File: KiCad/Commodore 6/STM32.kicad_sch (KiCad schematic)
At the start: 13 parts, among them J1 472192001, U1 STM32H562RIT6, U2 STM32H7A3RIT6

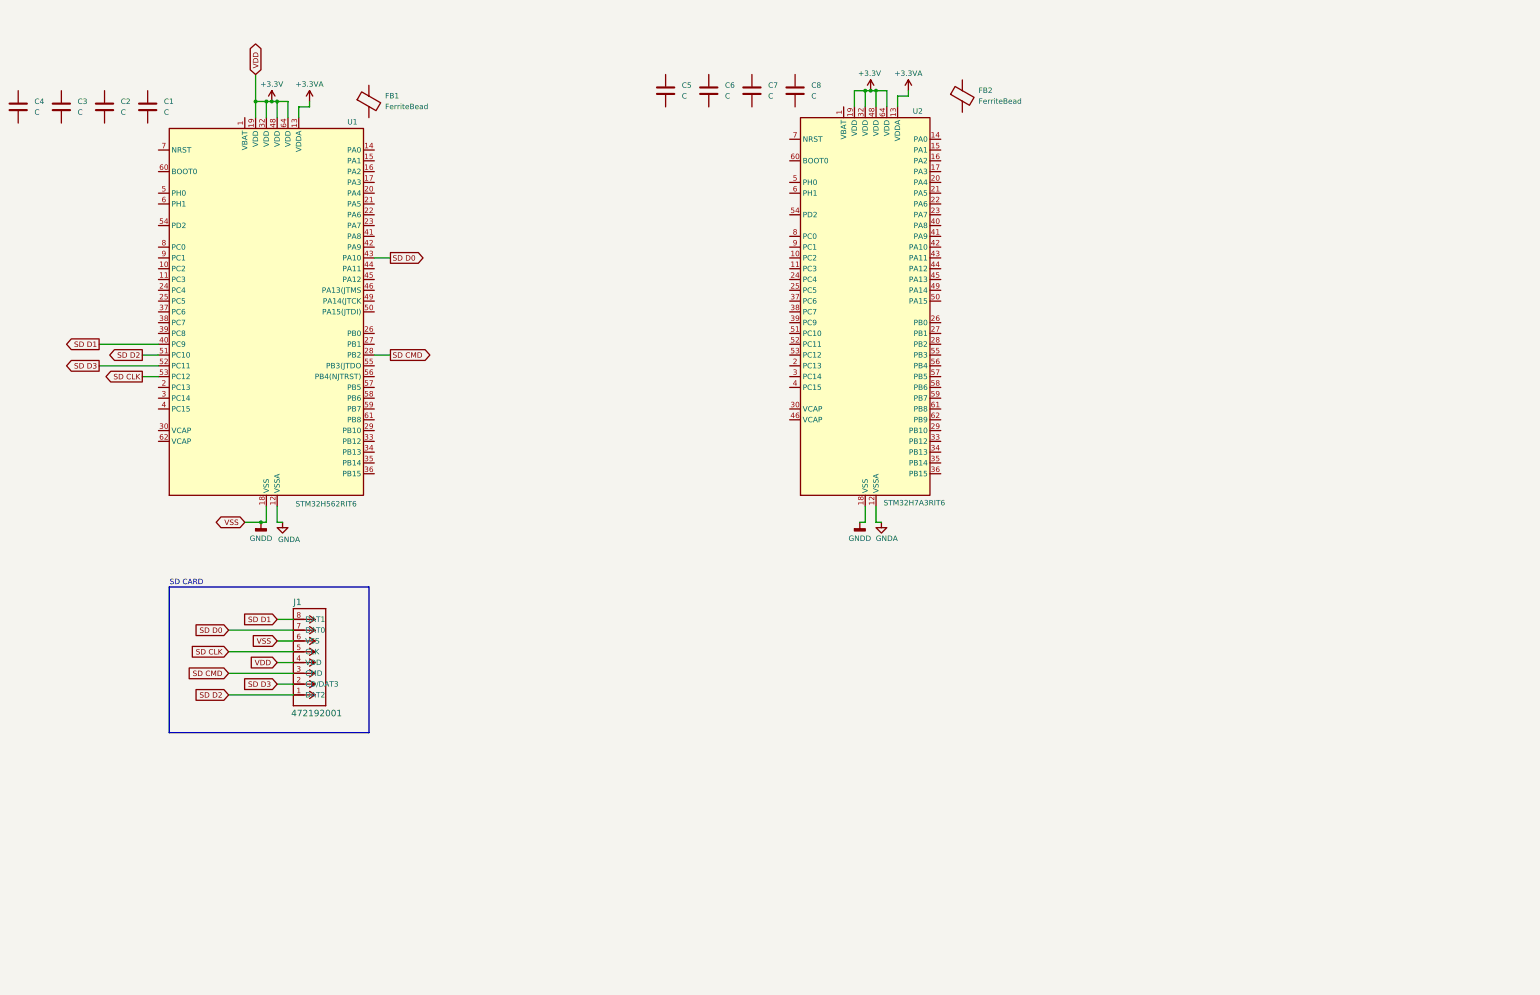
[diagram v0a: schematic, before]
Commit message: Added Ferite Bead
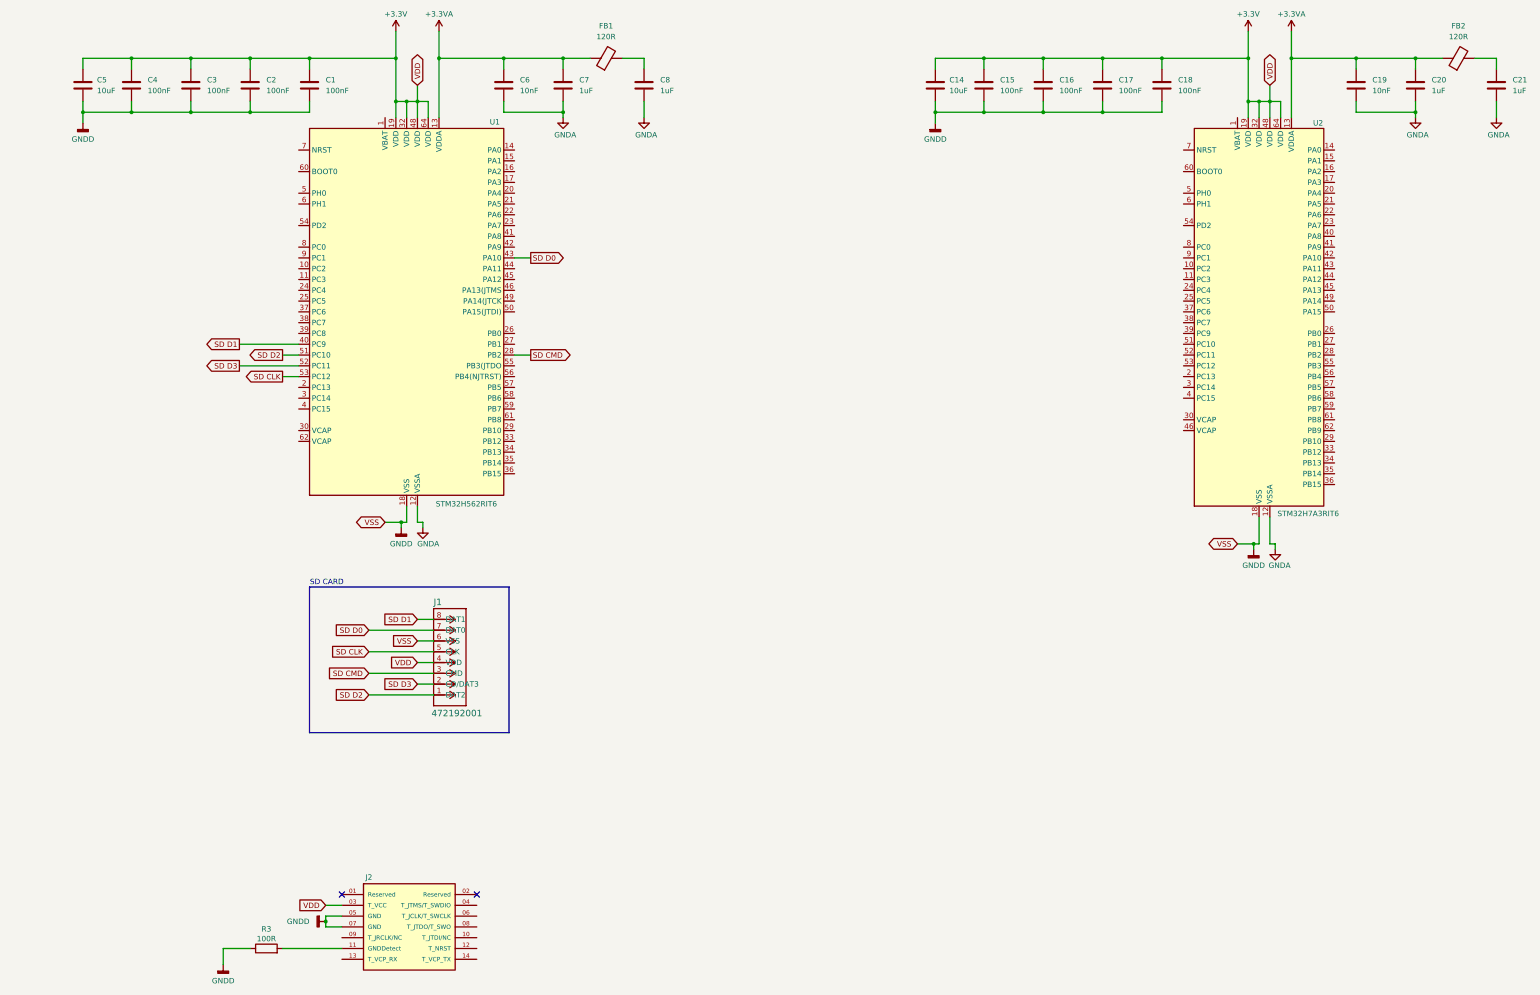
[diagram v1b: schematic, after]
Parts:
- added C14: 10uF, symbol Device:C
- added C15, C16, C17, C18: 100nF, symbol Device:C
- added C19: 10nF, symbol Device:C
- added C20, C21: 1uF, symbol Device:C
- added J2: FTSH-107-01-L-DV-K-A, FTSH-107-01-L-DV-K-A:SAMTEC_FTSH-107-01-L-DV-K-A, symbol FTSH_107_01_L_DV_K_A SWD Connecter:FTSH-107-01-L-DV-K-A
- added R3: 100R, symbol Device:R
- C1, C2, C3, C4: value C -> 100nF
- C5: value C -> 10uF
- C6: value C -> 10nF
- C7, C8: value C -> 1uF
- FB1, FB2: value FerriteBead -> 120R
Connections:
- net +3.3V: now also C1.1, C2.1, C3.1, C4.1, C5.1, C14.1, C15.1, C16.1, C17.1, C18.1, J2.03 (T_VCC)
- net +3.3VA: now also C6.1, C7.1, FB1.1, FB2.1, C19.1, C20.1
- net GNDA: now also C6.2, C7.2, C8.2, C19.2, C20.2, C21.2
- net GNDD: now also C1.2, C2.2, C3.2, C4.2, C5.2, C14.2, C15.2, C16.2, C17.2, C18.2, J2.05 (GND), J2.07 (GND), R3.1
- net at FB2.2: now also C21.1
- net at C8.1: now also FB1.2
- new net: J2.11 (GNDDetect), R3.2
- no-connect marks 0 -> 2
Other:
- moved on the sheet: C1, C2, C3, C4, C5, FB1, J1, U1, U2
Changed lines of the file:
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@@
 	(generator "eeschema")
 	(generator_version "9.0")
-	(paper "A3")
+	(paper "A2")

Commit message: I'm Tired
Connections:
- net T_SWDIO: now reaches U1.46 (PA13(JTMS)
- net T_SWDIO: now also J2.04 (T_JTMS/T_SWDIO)
- net T_SWCLK: now reaches U1.49 (PA14(JTCK)
- net T_SWCLK: now also J2.06 (T_JCLK/T_SWCLK)
- net T_JTDI: now reaches U1.50 (PA15(JTDI))
- net T_JTDI: now also J2.10 (T_JTDI/NC)
- net T_SWO: now reaches U1.55 (PB3(JTDO)
- net T_SWO: now also J2.08 (T_JTDO/T_SWO)
- net T_NRST: now reaches U1.7 (NRST)
- net T_NRST: now also J2.12 (T_NRST)
- net T_VCP_RX: now reaches J2.13 (T_VCP_RX)
- net T_VCP_TX: now reaches J2.14 (T_VCP_TX)
- no-connect marks 2 -> 3
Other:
- moved on the sheet: R3

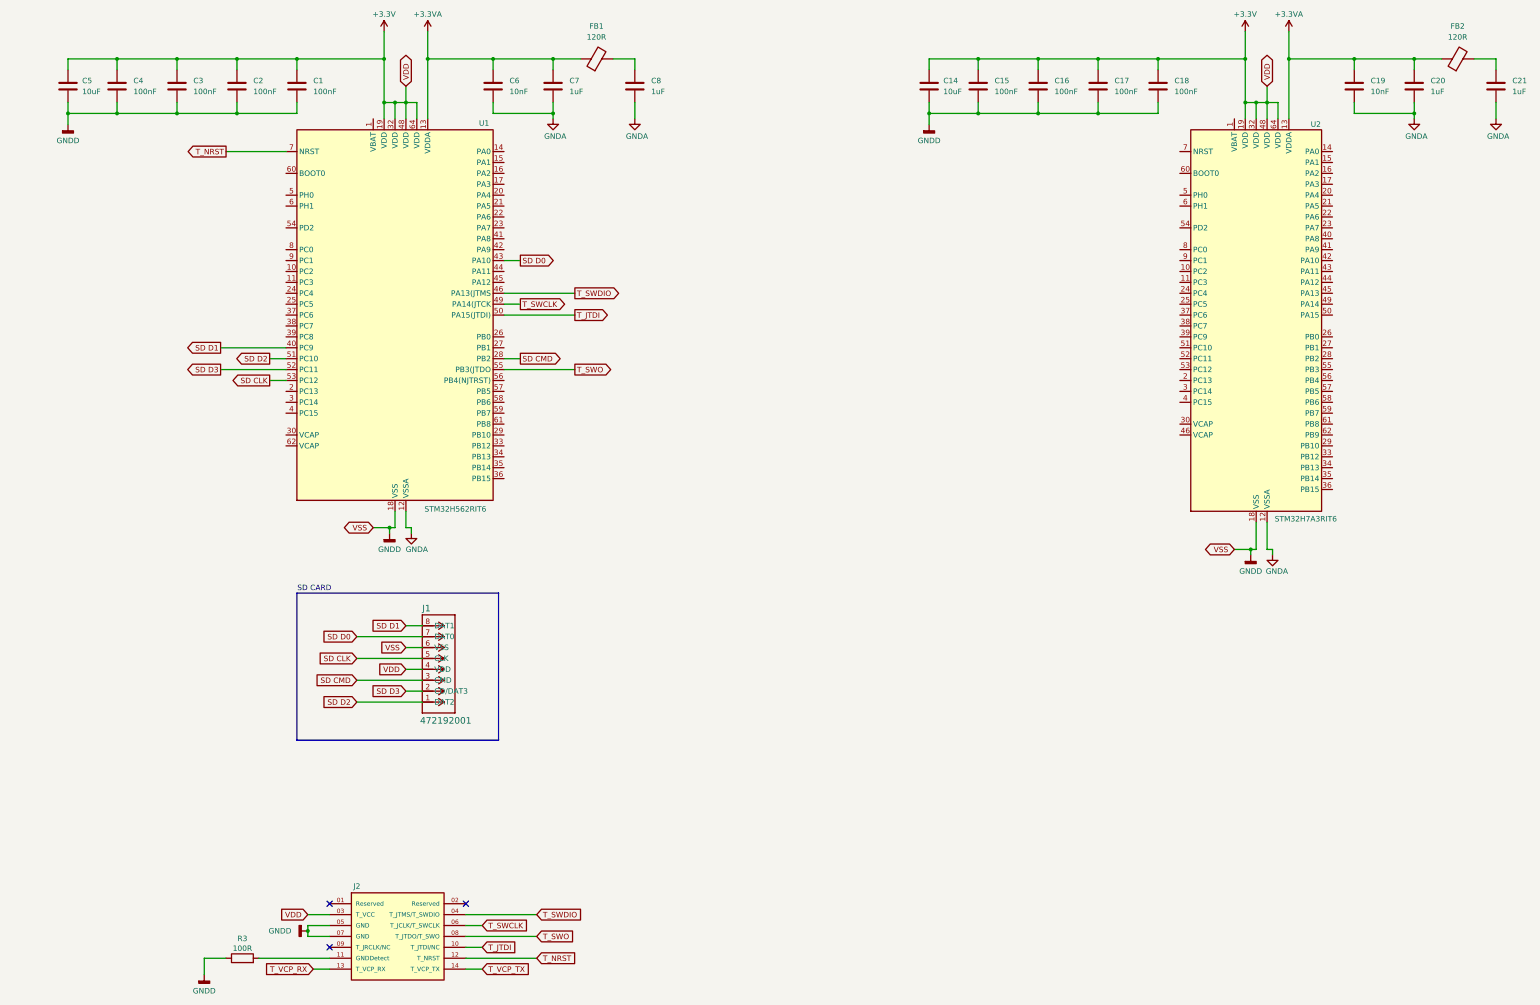
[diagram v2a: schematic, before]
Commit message: Fixed Ferrite bead and SD card
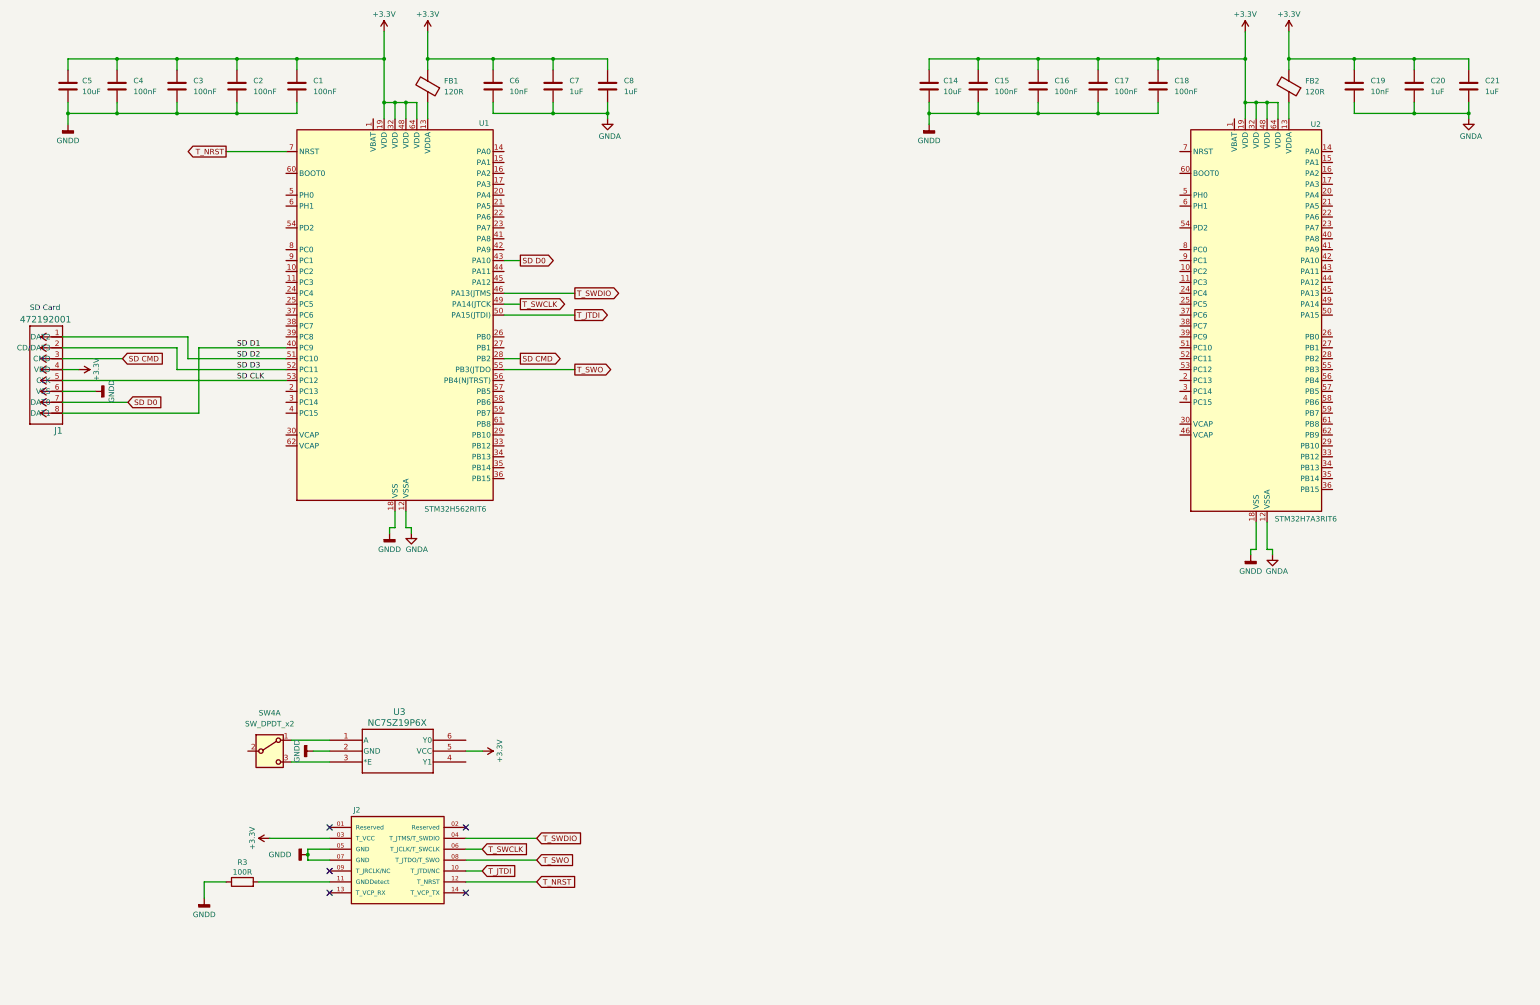
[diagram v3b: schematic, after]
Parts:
- added SW4: SW_DPDT_x2, symbol Switch:SW_DPDT_x2
- added U3: NC7SZ19P6X, SOT363-6_FAS, symbol NC7SZ19P6X Demultiplexer:NC7SZ19P6X
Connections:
- net +3.3V: now also C19.1, C20.1, C21.1, C6.1, C7.1, C8.1, FB1.2, FB2.2, U3.5 (VCC)
- net GNDD: now also U3.2 (GND)
- removed net +3.3VA: C19.1, C20.1, C6.1, C7.1, FB1.1, FB2.1, U1.13 (VDDA), U2.13 (VDDA)
- net T_VCP_RX: no longer names the net of J2.13 (T_VCP_RX)
- net T_VCP_TX: no longer names the net of J2.14 (T_VCP_TX)
- new net: FB2.1, U2.13 (VDDA)
- new net: FB1.1, U1.13 (VDDA)
- new net: SW4.1 (A), U3.1 (A)
- new net: SW4.3 (C), U3.3 (*E)
- no-connect marks 3 -> 5
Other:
- note added: "SD Card"
- note removed: "SD CARD"
- moved on the sheet: C21, C8, FB1, FB2, J1, J2, R3
